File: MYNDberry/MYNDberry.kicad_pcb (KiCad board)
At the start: 2 copper layers, 83.8 x 45.7 mm, 38 parts, among them CN1 1.0-4P WT, J1 Power Header, J2 Audio Header, J3 MCU/Debug Header, J4 RPi Peripheral Header, J5 Conn_01x09, J6 Conn_01x09, J7 I2S Header, J8 Conn_01x03, Q1 AO3400A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

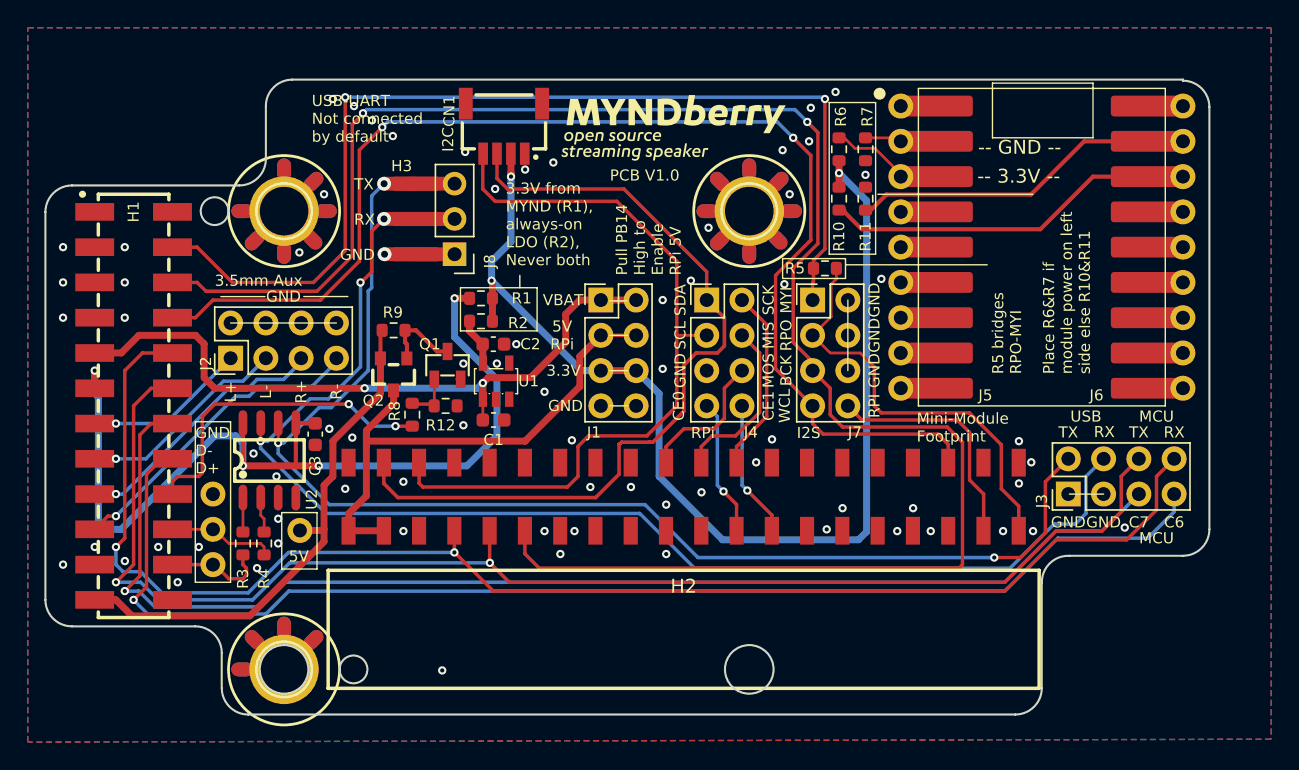
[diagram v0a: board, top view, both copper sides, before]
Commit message: Created new version using through hole headers for RasPi
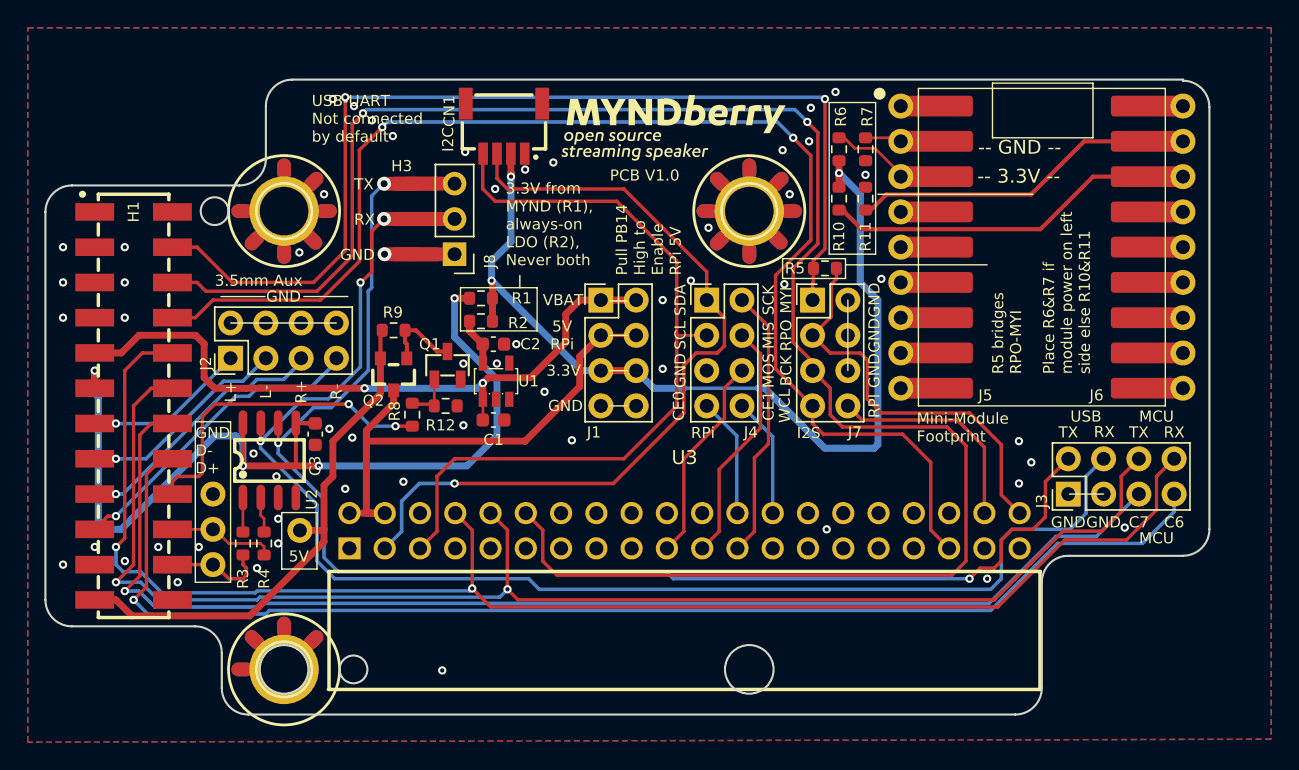
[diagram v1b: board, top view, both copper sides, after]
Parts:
- removed H2: RPi, Library:2x40_2.54mm_Female_SMT_Vertical
- added U3: HC-PM254-8.5H-2X20PW, easyeda2kicad:HDR-TH_40P-P2.54-H-F-R2-C20-S2.54-N, F.Cu at (127.4, 105.4)
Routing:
- net (no net): track 7.54 -> 19.8 mm
- net GND: track 18.3 -> 5.95 mm, vias 73 -> 59
- net /3.3V_AUX: track 79.9 -> 68.5 mm
- net /SCLK: track 13.4 -> 19.6 mm
- net /DBG_RX: track 104.7 -> 109.9 mm
- net /MISO: track 12.5 -> 17.6 mm
- net /MOSI: track 10.2 -> 15.0 mm
- net /I2S_WCLK: track 90.7 -> 95.4 mm
- net /DBG_TX: track 100.5 -> 104.5 mm
- net /UART0_TX: track 104.5 -> 107.7 mm
- net /UART0_RX: track 99.9 -> 103.1 mm
- net /I2S_BCLK: track 132.8 -> 134.2 mm
- net /I2S_DIN: track 17.1 -> 15.8 mm
- net /CE0: track 9.88 -> 8.64 mm, vias 1 -> 0
- net /I2S_DOUT: track 30.5 -> 29.2 mm
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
